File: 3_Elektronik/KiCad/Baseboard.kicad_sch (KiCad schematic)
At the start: 76 parts, among them J1 Conn_02x10_Odd_Even, J2 Conn_02x10_Odd_Even, J3 Conn_02x10_Odd_Even, J4 Conn_02x10_Odd_Even, J5 Conn_01x04_Pin, J6 693072010801, J7 629722000214, Q1 2N7002K, Q2 2N7002K, SW2 434331013822, SW3 434331013822, U1 LSM6DSV320XTR, U2 TPS7B8601QDDARQ1, U3 TCAN334, U4 ESP32-S3-WROOM-1, U5 LSM6DSO32XTR, U6 DPS310, U7 LIS3MDL, U8 CH224A

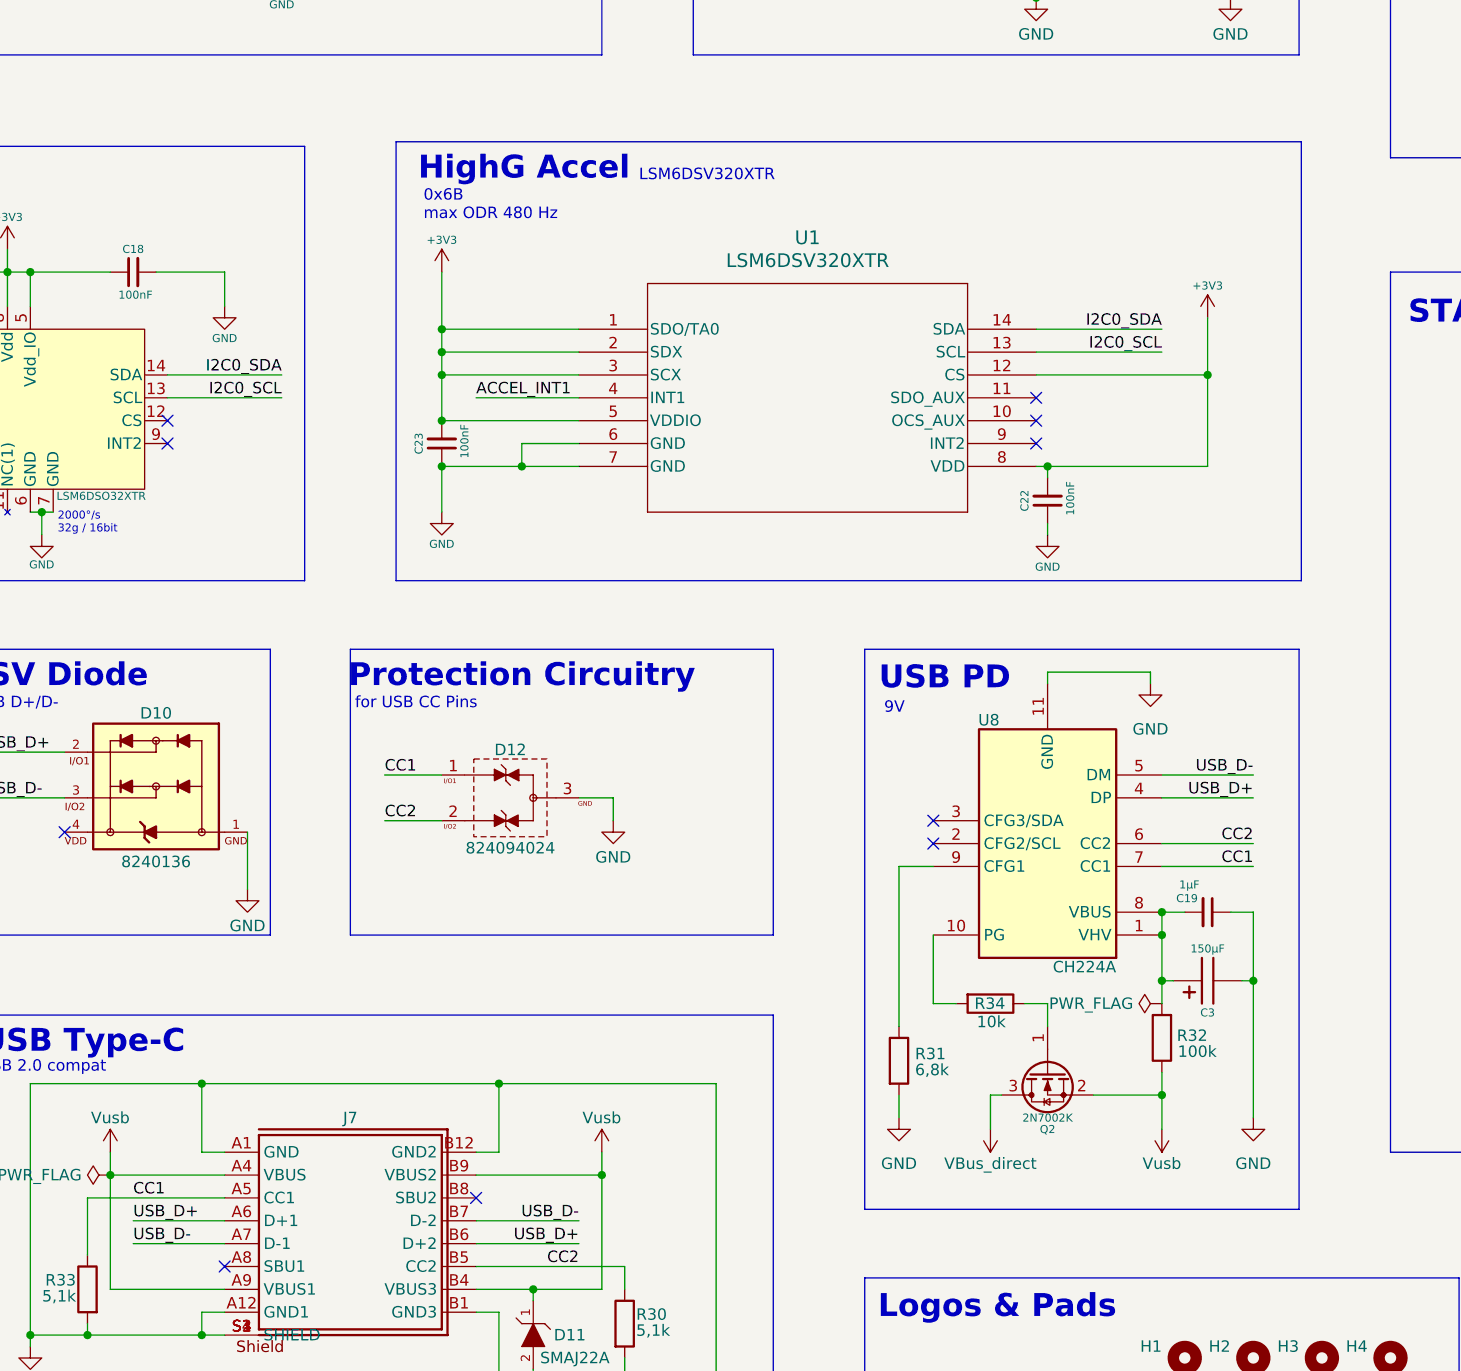
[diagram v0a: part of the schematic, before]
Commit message: fix: :bug: USB PD being 5V
USB PD is now set to 9V via I/O level configuration
as described in chapter 5.2.2 and table 5-2 in the
CH224A datasheet:

| CFG1 | CFG2 | CFG3 | Voltage |
|:----:|:----:|:---:-|--------:|
| 0    | 0    | 0    |  9V     |
| 0    | 0    | 1    | 12V     |
| 0    | 1    | 1    | 20V     |
| 0    | 1    | 0    | 28V     |
| 1    | X    | X    |  5V     |
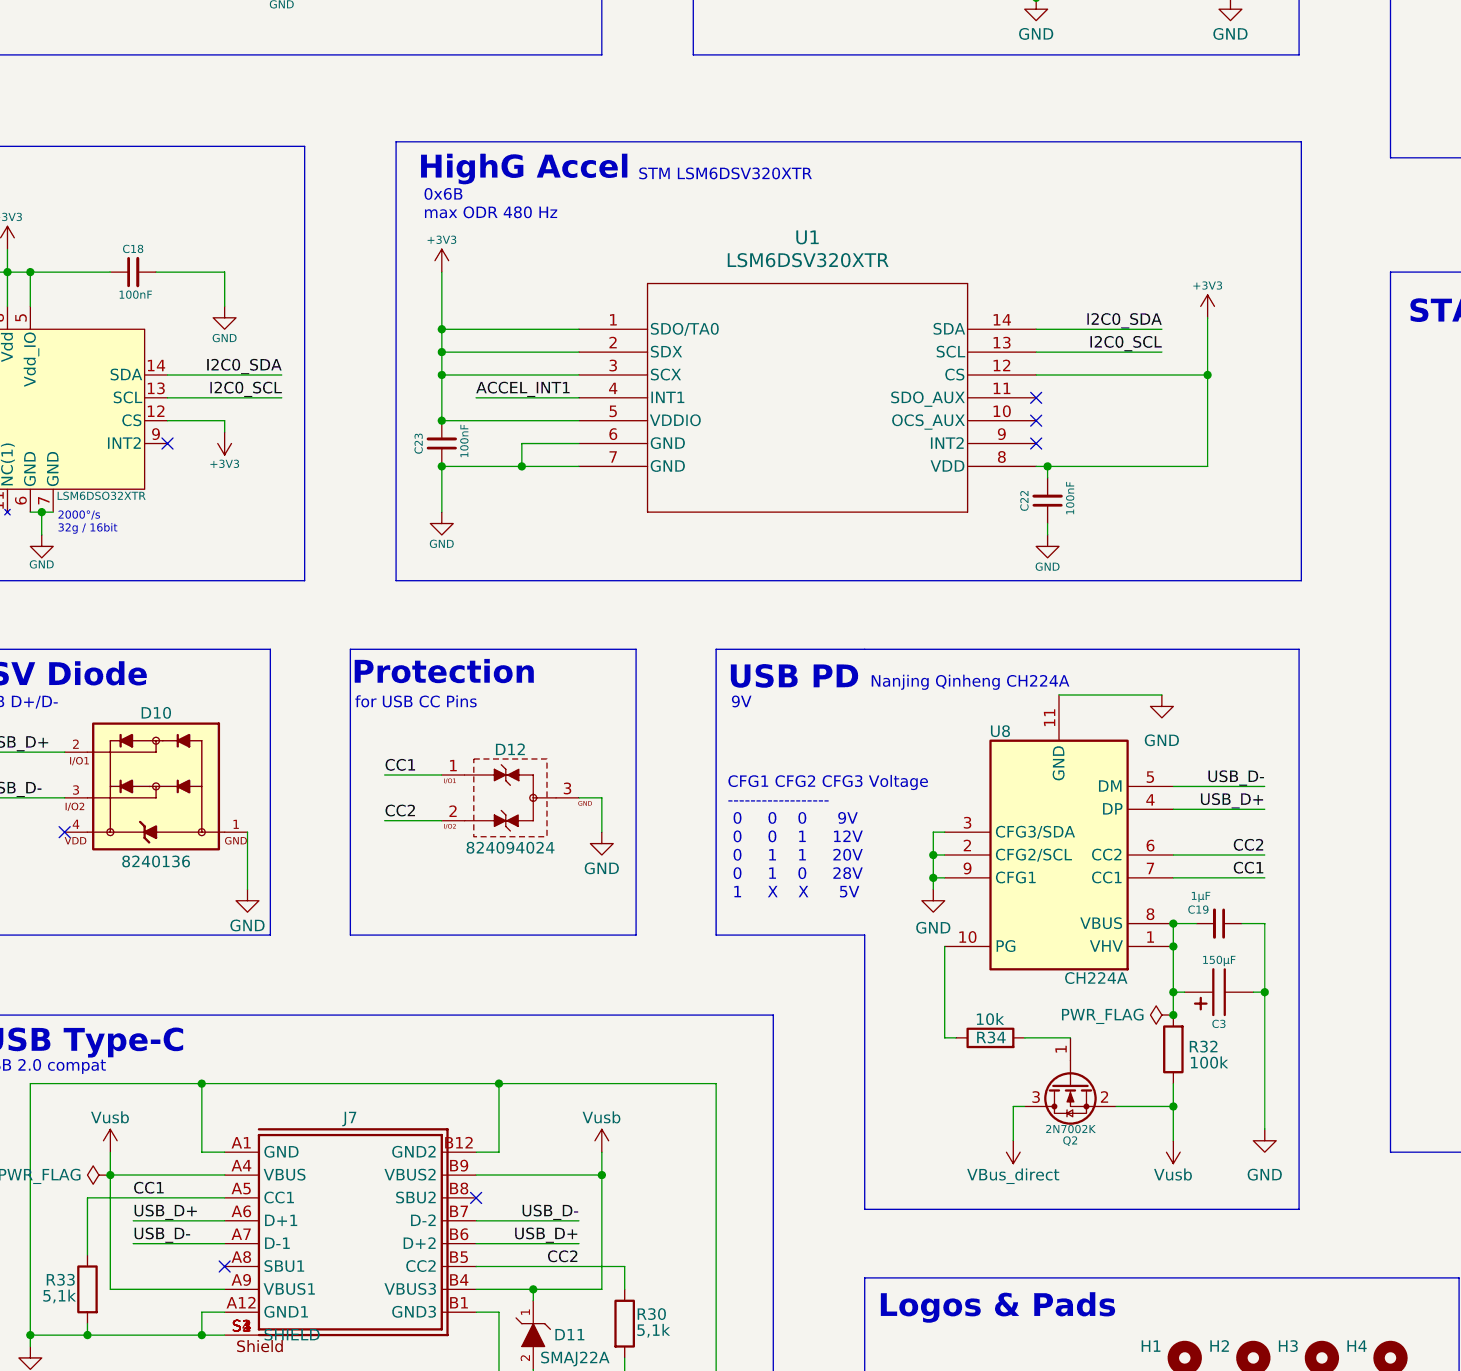
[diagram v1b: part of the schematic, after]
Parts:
- removed R31: 6,8k, Resistor_SMD:R_0603_1608Metric, symbol Device:R
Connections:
- net +3V3: now also U5.12 (CS)
- net GND: now also U8.2 (CFG2/SCL), U8.3 (CFG3/SDA), U8.9 (CFG1)
- net at R34.1: now also U8.10 (PG); no longer Q2.1 (G)
- net at R34.2: now also Q2.1 (G); no longer U8.10 (PG)
- no-connect marks 15 -> 12
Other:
- note added: "CFG1 CFG2 CFG3 Voltage ------------------ 0 0 0 9V 0 0 1 12V 0 1 1 20V 0 1 0 28V 1 X X 5V"
- note added: "Nanjing Qinheng CH224A"
- note added: "Protection"
- note added: "STM LSM6DSV320XTR"
- note removed: "LSM6DSV320XTR"
- note removed: "Protection Circuitry"
- moved on the sheet: C19, C3, Q2, R32, R34, U8

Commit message: style: :art: cleanup pcb
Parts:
- R23: value 390R -> 4,7k
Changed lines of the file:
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@@
 	)
 	(junction
-		(at 58.42 215.9)
-		(diameter 0)
-		(color 0 0 0 0)
-	)
-	(junction
 		(at 128.27 110.49)
 		(diameter 0)
@@
 	)
 	(junction
+		(at 303.53 191.77)
+		(diameter 0)
+		(color 0 0 0 0)
+	)
+	(junction
 		(at 303.53 172.72)
 		(diameter 0)
@@
 	(wire
 		(pts
-			(xy 59.69 215.9) (xy 58.42 215.9)
-		)
-		(stroke
-			(width 0)
-			(type default)
-		)
-	)
-	(wire
-		(pts
 			(xy 64.77 198.12) (xy 64.77 200.66)
 		)
@@
 	(wire
 		(pts
+			(xy 34.29 215.9) (xy 58.42 215.9)
+		)
+		(stroke
+			(width 0)
+			(type default)
+		)
+	)
+	(wire
+		(pts
 			(xy 88.9 256.54) (xy 105.41 256.54)
 		)
@@
 	(wire
 		(pts
-			(xy 303.53 191.77) (xy 300.99 191.77)
-		)
-		(stroke
-			(width 0)
-			(type default)
-		)
-	)
-	(wire
-		(pts
 			(xy 294.64 111.76) (xy 294.64 119.38)
 		)
@@
 	(wire
 		(pts
+			(xy 303.53 191.77) (xy 300.99 191.77)
+		)
+		(stroke
+			(width 0)
+			(type default)
+		)
+	)
+	(wire
+		(pts
 			(xy 195.58 265.43) (xy 195.58 267.97)
 		)
@@
 	(wire
 		(pts
-			(xy 34.29 215.9) (xy 58.42 215.9)
-		)
-		(stroke
-			(width 0)
-			(type default)
-		)
-	)
-	(wire
-		(pts
 			(xy 157.48 110.49) (xy 157.48 109.22)
 		)
@@
 	(symbol
 		(lib_id "power:GND")
-		(at 300.99 191.77 0)
+		(at 303.53 191.77 0)
 		(unit 1)
 		(body_style 1)
@@
 		(dnp no)
 		(property "Reference" "#PWR06"
-			(at 300.99 198.12 0)
+			(at 303.53 198.12 0)
 			(hide yes)
 			(show_name no)
@@
 		)
 		(property "Value" "GND"
-			(at 300.736 196.342 0)
+			(at 303.276 196.342 0)
 			(show_name no)
 			(do_not_autoplace no)
@@
 		)
 		(property "Footprint" ""
-			(at 300.99 191.77 0)
+			(at 303.53 191.77 0)
 			(hide yes)
 			(show_name no)
@@
 		)
 		(property "Datasheet" ""
-			(at 300.99 191.77 0)
+			(at 303.53 191.77 0)
 			(hide yes)
 			(show_name no)
@@
 		)
 		(property "Description" "Power symbol creates a global label with name \"GND\" , ground"
-			(at 300.99 191.77 0)
+			(at 303.53 191.77 0)
 			(hide yes)
 			(show_name no)
@@
 			)
 		)
-		(property "Value" "390R"
+		(property "Value" "4,7k"
 			(at 218.694 49.53 90)
 			(show_name no)

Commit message: chore: update after review
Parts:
- removed C11: 100nF, Capacitor_SMD:C_0603_1608Metric, symbol Device:C_Small
- added C25: 10µF, Capacitor_SMD:C_0603_1608Metric, symbol Device:C_Small
- Q2: value 2N7002K -> DMP3099L; symbol Transistor_FET:2N7002K -> Transistor_FET:DMP3099L; LCSC_PTNBR C3008053 -> (none)
- R18, R21, R22: value 390R -> 2,7k
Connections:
- net +3V3: now also C25.1
- net GND: now also C25.2
- net IO0: now also SW3.3, SW3.4, SW3.5, SW3.6; no longer SW3.1, SW3.2
- new net: R23.2, SW3.1, SW3.2
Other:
- moved on the sheet: SW3

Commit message: style: :art: split schematics into subpages
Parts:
- removed BZ1: WST-0904T, AUXSPACE:Buzzer_WST-0906T, symbol Device:Buzzer
- removed C10, C17, C19, C21: 1µF, Capacitor_SMD:C_0603_1608Metric, symbol Device:C_Small
- removed C12, C13, C14, C16, C18, C20, C22, C23, C24, C4, C8, C9: 100nF, Capacitor_SMD:C_0603_1608Metric, symbol Device:C_Small
- removed C15, C25, C7: 10µF, Capacitor_SMD:C_0603_1608Metric, symbol Device:C_Small
- removed C3: 150 µF, AUXSPACE:CP_Wurth_WCAP-ASLL-D6.3L5.5, symbol AUXSPACE:D6.3L5.5_865060243005
- removed C5, C6: 100nF, Capacitor_SMD:C_0603_1608Metric, symbol Device:C
- removed D10: 8240136, AUXSPACE:WE-TVS_SOT143-4L, symbol AUXSPACE:WE-TVS-HS_SOT143-4L_8240136
- removed D11: SMAJ22A, AUXSPACE:WE-TVS_SMAJ22A, symbol AUXSPACE:WE-TVSP_DO-214AC_400W_UNI
- removed D12: 824094024, AUXSPACE:WE-TVS_824094024_SOT23-3L, symbol AUXSPACE:SOT23-3L_824094024
- removed D3, D4, D5: grün, LED_SMD:LED_0603_1608Metric, symbol Device:LED
- removed J5: Conn_01x04_Pin, symbol Connector:Conn_01x04_Pin
- removed J6: 693072010801, AUXSPACE:J_Wurth_WR-CRD_693072010801, symbol AUXSPACE:693072010801
- removed J7: 629722000214, AUXSPACE:J_Wurth_WR-USB_629722000214, symbol AUXSPACE:629722000214
- removed Q1: 2N7002K, Package_TO_SOT_SMD:SOT-23, symbol Transistor_FET:2N7002K
- removed Q2: DMP3099L, Package_TO_SOT_SMD:SOT-23, symbol Transistor_FET:DMP3099L
- removed R10, R11, R14, R16, R23, R9: 4,7k, Resistor_SMD:R_0603_1608Metric, symbol Device:R_Small
- removed R12: 10k, Resistor_SMD:R_0603_1608Metric, symbol Device:R_Small
- removed R15, R4: 11k, Resistor_SMD:R_0603_1608Metric, symbol Device:R_Small
- removed R17, R2: 62R, Resistor_SMD:R_0603_1608Metric, symbol Device:R_Small
- removed R18, R21, R22, R6: 2,7k, Resistor_SMD:R_0603_1608Metric, symbol Device:R_Small
- removed R19, R20: 22R, Resistor_SMD:R_0603_1608Metric, symbol Device:R_Small
- removed R30, R33: 5,1k, Resistor_SMD:R_0603_1608Metric, symbol Device:R
- removed R32: 100k, Resistor_SMD:R_0603_1608Metric, symbol Device:R
- removed R34: 10k, Resistor_SMD:R_0603_1608Metric, symbol Device:R
- removed SW2, SW3: 434331013822, AUXSPACE:SW_Wurth_WS-TASU_434331013822, symbol AUXSPACE:434331013822
- removed U1: LSM6DSV320XTR, AUXSPACE:LGA-14L_2p5X3X0p83_STM, symbol AUXSPACE:LSM6DSV320XTR
- removed U2: TPS7B8601QDDARQ1, AUXSPACE:Texas_R-PDSO-G8_EP2.95x4.9mm_Mask2.4x3.1mm_ThermalVias, symbol AUXSPACE:TPS7B8601QDDARQ1
- removed U3: TCAN334, Package_SO:SOIC-8_3.9x4.9mm_P1.27mm, symbol AUXSPACE:TCAN334
- removed U4: ESP32-S3-WROOM-1, AUXSPACE:ESP32-S3-WROOM-1, symbol AUXSPACE:ESP32-S3-WROOM-1
- removed U5: LSM6DSO32XTR, AUXSPACE:LGA_O32XTR_STM, symbol AUXSPACE:LSM6DSO32XTR
- removed U6: DPS310, AUXSPACE:DPS310, symbol AUXSPACE:DPS310
- removed U7: LIS3MDL, Package_LGA:LGA-12_2x2mm_P0.5mm, symbol Sensor_Magnetic:LIS3MDL
- removed U8: CH224A, AUXSPACE:ESSOP-10-1EP_3.9x5.0mm_P1mm_EP2.1x3.3mm, symbol CH224A:CH224A
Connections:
- net Bat on ext renamed Bat_on_ext
- net Power Fault renamed Power_Fault
- no-connect marks 12 -> 0
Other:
- note removed: "0x1C"
- note removed: "0x6A max ODR 6664Hz"
- note removed: "0x6B max ODR 480 Hz"
- note removed: "0x77"
- note removed: "2000°/s 32g / 16bit"
- note removed: "3,3V Spannungsversorgung"
- note removed: "9V"
- note removed: "ADC Vref=1,1V Input signal attenuation set by firmware"
- note removed: "BARO"
- note removed: "BOOTSEL"
- note removed: "BUZZER"
- note removed: "CAN"
- note removed: "CFG1 CFG2 CFG3 Voltage ------------------ 0 0 0 9V 0 0 1 12V 0 1 1 20V 0 1 0 28V 1 X X 5V"
- note removed: "HighG Accel"
- note removed: "IMU"
- note removed: "Infineon DPS310 or DPS368"
- note removed: "MAGNETOMETER"
- note removed: "Microcontroller"
- note removed: "Nanjing Qinheng CH224A"
- note removed: "POWER"
- note removed: "Protection"
- note removed: "Pull-Ups"
- note removed: "SD-Card"
- note removed: "STM LIS3MDL"
- note removed: "STM LSM6DS032x"
- note removed: "STM LSM6DSV320XTR"
- note removed: "Status LEDs"
- note removed: "TSV Diode"
- note removed: "UART/Programming"
- note removed: "USB 2.0 compat"
- note removed: "USB D+/D-"
- note removed: "USB PD"
- note removed: "USB Type-C"
- note removed: "for USB CC Pins"
- note removed: "when using the SDIO protocol use ESP internal PullUp resitors @ each pin accept CLK"
- moved on the sheet: H1, H2, H3, H4, J1, J2, J3, J4, Logo1, Logo2
